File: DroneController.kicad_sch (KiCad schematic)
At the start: 50 parts, among them J1 Connector, J2 Connector, J3 Connector, P1 USB_C_Plug, Q2 AO3400A, SW1 SW_SPDT, U2 W25Q16JVSS, U3 BMP280, U4 MPU-6500, U6 L86-M33, U7 915MHz, U9 AP7361C-33E, X1 X322512MSB4SI

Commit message: Fixed GPS wiring
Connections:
- net 3.3V is gone; now on net +3.3V: U6.4 (VCC)
- net USART1_RX renamed MCU_RX1
- net MCU_RX1: now also U6.2 (TXD1); no longer U6.1 (RXD1)
- net USART1_TX renamed MCU_TX1
- net MCU_TX1: now also U6.1 (RXD1); no longer U6.2 (TXD1)
- net USART2_RX renamed MCU_RX2
- net MCU_RX2: now also J1.2 (Pin_2); no longer J1.1 (Pin_1)
- net USART2_TX renamed MCU_TX2
- net MCU_TX2: now also J1.1 (Pin_1); no longer J1.2 (Pin_2)
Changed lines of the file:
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@@
 	)
 	(junction
-		(at 60.96 25.4)
-		(diameter 0)
-		(color 0 0 0 0)
-	)
-	(junction
 		(at 157.48 40.64)
 		(diameter 0)
@@
 	)
 	(junction
+		(at 62.23 25.4)
+		(diameter 0)
+		(color 0 0 0 0)
+	)
+	(junction
 		(at 161.29 123.19)
 		(diameter 0)
@@
 	(wire
 		(pts
-			(xy 60.96 22.86) (xy 60.96 25.4)
+			(xy 62.23 22.86) (xy 62.23 25.4)
 		)
 		(stroke
@@
 	(wire
 		(pts
+			(xy 62.23 22.86) (xy 60.96 22.86)
+		)
+		(stroke
+			(width 0)
+			(type default)
+		)
+	)
+	(wire
+		(pts
 			(xy 217.17 104.14) (xy 220.98 104.14)
 		)
@@
 	(wire
 		(pts
+			(xy 147.32 72.39) (xy 137.16 72.39)
+		)
+		(stroke
+			(width 0)
+			(type default)
+		)
+	)
+	(wire
+		(pts
 			(xy 53.34 93.98) (xy 53.34 91.44)
 		)
@@
 		)
 	)
+	(wire
+		(pts
+			(xy 62.23 25.4) (xy 60.96 25.4)
+		)
+		(stroke
+			(width 0)
+			(type default)
+		)
+	)
 	(polyline
 		(pts
@@
 		)
 	)
-	(wire
-		(pts
-			(xy 62.23 25.4) (xy 60.96 25.4)
-		)
-		(stroke
-			(width 0)
-			(type default)
-		)
-	)
 	(polyline
 		(pts
@@
 		)
 	)
-	(label "USART1_RX"
+	(label "MCU_TX1"
 		(at 50.8 83.82 0)
 		(effects
@@
 		)
 	)
+	(label "MCU_TX1"
+		(at 266.7 38.1 0)
+		(effects
+			(font
+				(size 1.27 1.27)
+			)
+			(justify left bottom)
+		)
+	)
 	(label "SPI5_NSS"
 		(at 266.7 50.8 0)
@@
 		)
 	)
+	(label "MCU_RX2"
+		(at 189.23 129.54 180)
+		(effects
+			(font
+				(size 1.27 1.27)
+			)
+			(justify right bottom)
+		)
+	)
 	(label "SPI2_SCK"
 		(at 266.7 22.86 0)
@@
 		)
 	)
-	(label "USART2_RX"
+	(label "MCU_RX1"
+		(at 50.8 86.36 0)
+		(effects
+			(font
+				(size 1.27 1.27)
+			)
+			(justify left bottom)
+		)
+	)
+	(label "MCU_RX2"
 		(at 266.7 88.9 0)
 		(effects
@@
 		)
 	)
-	(label "USART1_TX"
-		(at 266.7 38.1 0)
-		(effects
-			(font
-				(size 1.27 1.27)
-			)
-			(justify left bottom)
-		)
-	)
 	(label "SPI1_NSS"
 		(at 104.14 125.73 180)
@@
 		)
 	)
-	(label "USART1_RX"
-		(at 266.7 35.56 0)
-		(effects
-			(font
-				(size 1.27 1.27)
-			)
-			(justify left bottom)
-		)
-	)
 	(label "SPI1_NSS"
 		(at 266.7 86.36 0)
@@
 		)
 	)
-	(label "USART2_TX"
+	(label "MCU_TX2"
 		(at 266.7 91.44 0)
 		(effects
@@
 		)
 	)
-	(label "USART2_RX"
+	(label "MCU_TX2"
 		(at 189.23 127 180)
 		(effects
@@
 		)
 	)
-	(label "USART2_TX"
-		(at 189.23 129.54 180)
+	(label "MCU_RX1"
+		(at 266.7 35.56 0)
 		(effects
 			(font
 				(size 1.27 1.27)
 			)
-			(justify right bottom)
+			(justify left bottom)
 		)
 	)
@@
 		)
 	)
-	(label "USART1_TX"
-		(at 50.8 86.36 0)
-		(effects
-			(font
-				(size 1.27 1.27)
-			)
-			(justify left bottom)
-		)
-	)
 	(label "SPI1_MISO"
 		(at 248.92 135.89 180)
@@
 	)
 	(symbol
+		(lib_id "power:+3.3V")
+		(at 50.8 66.04 0)
+		(unit 1)
+		(exclude_from_sim no)
+		(in_bom yes)
+		(on_board yes)
+		(dnp no)
+		(fields_autoplaced yes)
+		(property "Reference" "#PWR035"
+			(at 50.8 69.85 0)
+			(effects
+				(font
+					(size 1.27 1.27)
+				)
+				(hide yes)
+			)
+		)
+		(property "Value" "+3.3V"
+			(at 50.8 60.96 0)
+			(effects
+				(font
+					(size 1.27 1.27)
+				)
+			)
+		)
+		(property "Footprint" ""
+			(at 50.8 66.04 0)
+			(effects
+				(font
+					(size 1.27 1.27)
+				)
+				(hide yes)
+			)
+		)
+		(property "Datasheet" ""
+			(at 50.8 66.04 0)
+			(effects
+				(font
+					(size 1.27 1.27)
+				)
+				(hide yes)
+			)
+		)
+		(property "Description" "Power symbol creates a global label with name \"+3.3V\""
+			(at 50.8 66.04 0)
+			(effects
+				(font
+					(size 1.27 1.27)
+				)
+				(hide yes)
+			)
+		)
+		(pin "1"
+		)
+		(instances
+			(project "DroneController"
+				(path "/89a72cea-fd24-4c2f-bde8-6b43291d77f4"
+					(reference "#PWR035")
+					(unit 1)
+				)
+			)
+		)
+	)
+	(symbol
 		(lib_name "0402,100nF_1")
 		(lib_id "PCM_JLCPCB-Capacitors:0402,100nF")
@@
 	)
 	(symbol
-		(lib_id "power:+BATT")
-		(at 50.8 66.04 0)
-		(unit 1)
-		(exclude_from_sim no)
-		(in_bom yes)
-		(on_board yes)
-		(dnp no)
-		(property "Reference" "#PWR042"
-			(at 50.8 69.85 0)
-			(effects
-				(font
-					(size 1.27 1.27)
-				)
-				(hide yes)
-			)
-		)
-		(property "Value" "3.3V"
-			(at 50.8 60.96 0)
-			(effects
-				(font
-					(size 1.27 1.27)
-				)
-			)
-		)
-		(property "Footprint" ""
-			(at 50.8 66.04 0)
-			(effects
-				(font
-					(size 1.27 1.27)
-				)
-				(hide yes)
-			)
-		)
-		(property "Datasheet" ""
-			(at 50.8 66.04 0)
-			(effects
-				(font
-					(size 1.27 1.27)
-				)
-				(hide yes)
-			)
-		)
-		(property "Description" "Power symbol creates a global label with name \"+BATT\""
-			(at 50.8 66.04 0)
-			(effects
-				(font
-					(size 1.27 1.27)
-				)
-				(hide yes)
-			)
-		)
-		(pin "1"
-		)
-		(instances
-			(project "DroneController"
-				(path "/89a72cea-fd24-4c2f-bde8-6b43291d77f4"
-					(reference "#PWR042")
-					(unit 1)
-				)
-			)
-		)
-	)
-	(symbol
 		(lib_id "PCM_JLCPCB-Capacitors:0402,100nF")
 		(at 158.75 55.88 270)
@@
 	(symbol
 		(lib_id "power:+3.3V")
-		(at 137.16 72.39 0)
+		(at 147.32 72.39 0)
 		(unit 1)
 		(exclude_from_sim no)
@@
 		(dnp no)
 		(property "Reference" "#PWR044"
-			(at 137.16 76.2 0)
+			(at 147.32 76.2 0)
 			(effects
 				(font
@@
 		)
 		(property "Value" "+3.3V"
-			(at 137.16 68.072 0)
+			(at 147.32 68.072 0)
 			(effects
 				(font
@@
 		)
 		(property "Footprint" ""
-			(at 137.16 72.39 0)
+			(at 147.32 72.39 0)
 			(effects
 				(font
@@
 		)
 		(property "Datasheet" ""
-			(at 137.16 72.39 0)
+			(at 147.32 72.39 0)
 			(effects
 				(font
@@
 		)
 		(property "Description" "Power symbol creates a global label with name \"+3.3V\""
-			(at 137.16 72.39 0)
+			(at 147.32 72.39 0)
 			(effects
 				(font

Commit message: DroneController: Improved clarity of silkscreen and added manual reset test pad for the MCU.
ESC Board: Modified Buck Converter, added SWD debugging, added ICs for BLDC control
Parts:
- removed R6: 75Ω, PCM_JLCPCB:R_0603, symbol PCM_JLCPCB-Resistors:0603,75Ω
- added R11: 200Ω, PCM_JLCPCB:R_0402, symbol PCM_JLCPCB-Resistors:0402,200Ω
- added TP1, TP2: TestPoint, symbol Connector:TestPoint
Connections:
- net +5V: now also R11.1
- net GND: now also TP2.1
- net at C27.1, U5.7 (NRST): now also TP1.1
- net at D3.2: now also R11.2
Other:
- note added: "Drone Controller"
- note removed: "Flight Controller"

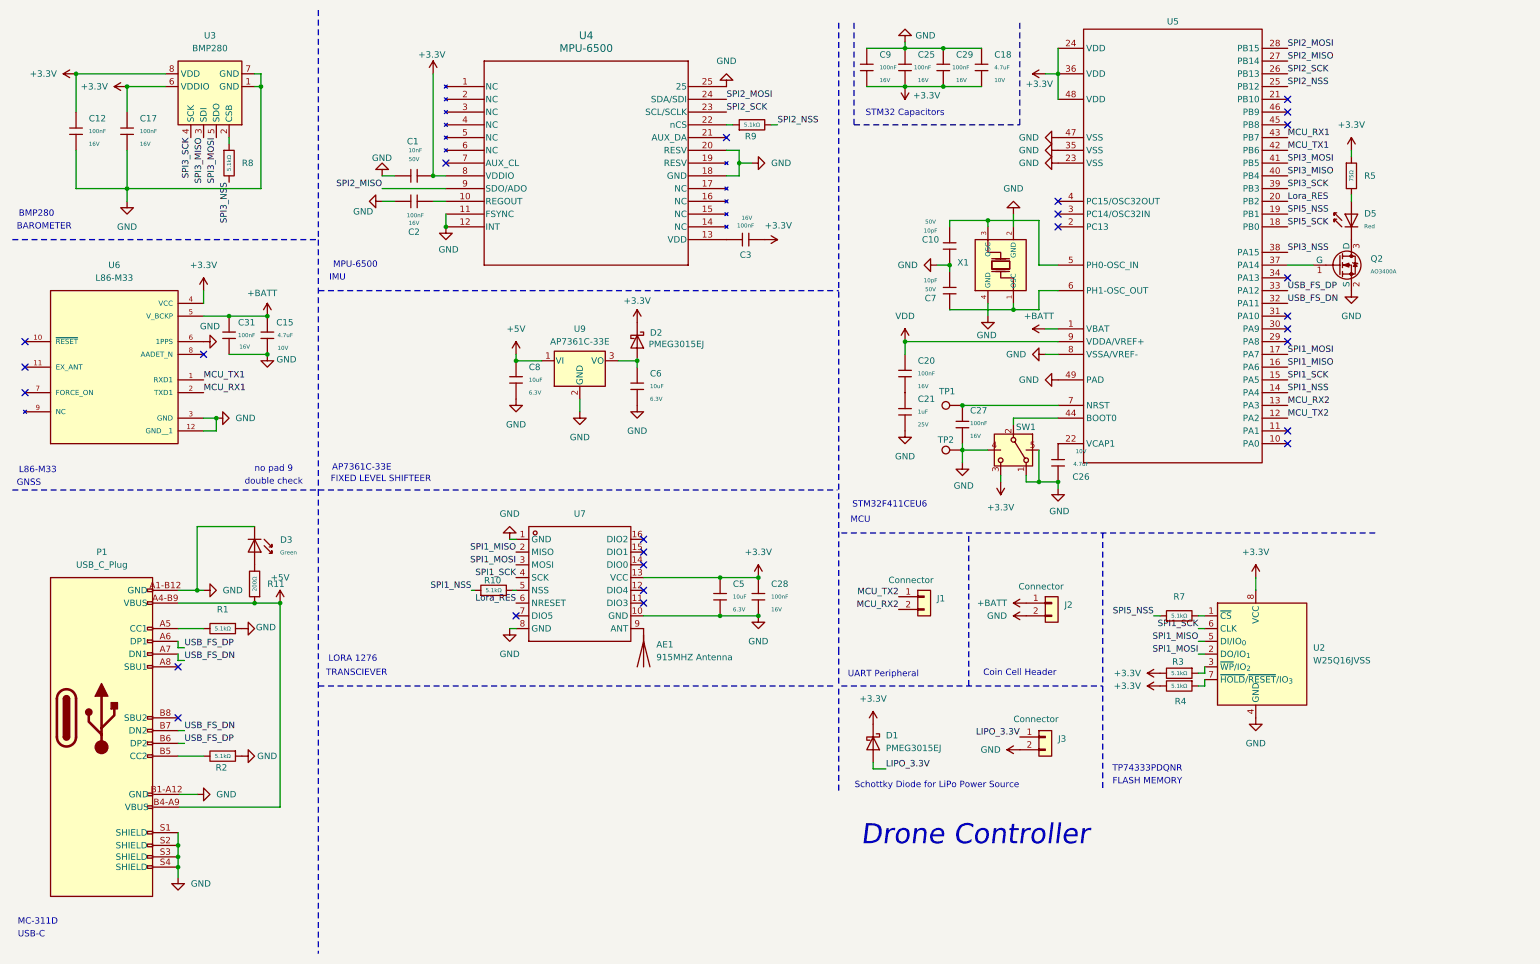
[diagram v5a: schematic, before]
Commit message: Added UART debugging for DroneController, repecced crystal oscillator.
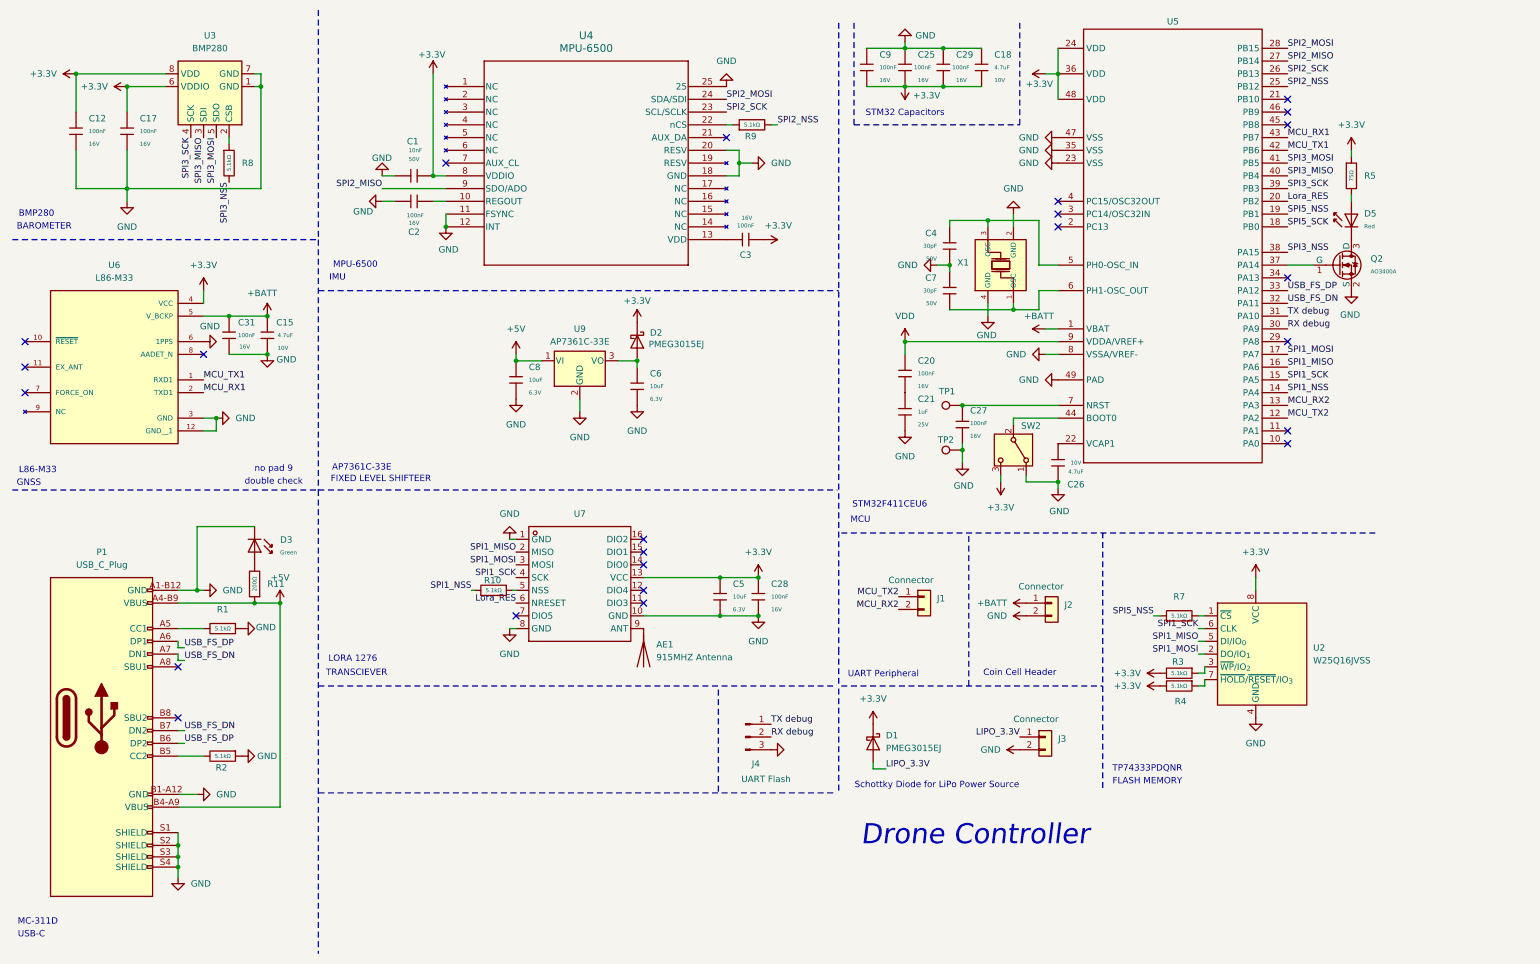
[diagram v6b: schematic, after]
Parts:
- removed C10, C7: 10pF, PCM_JLCPCB:C_0402, symbol PCM_JLCPCB-Capacitors:0402,10pF
- removed SW1: SW_SPDT, Switches:SW-SMD_MSK12CO2, symbol Switch:SW_SPDT
- added C4, C7: 30pF, PCM_JLCPCB:C_0402, symbol PCM_JLCPCB-Capacitors:0402,30pF
- added J4: UART Flash, Connector_PinHeader_1.00mm:PinHeader_1x03_P1.00mm_Vertical, symbol Connector:Conn_01x03_Pin
- added SW2: SW_SPDT, symbol Switch:SW_SPDT
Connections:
- net +3.3V: now also SW2.3 (C)
- net GND: now also C4.2, C7.1, J4.3 (Pin_3), SW2.1 (A)
- net at U5.6 (PH1-OSC_OUT), X1.1 (OSC): now also C7.2
- net at U5.5 (PH0-OSC_IN), X1.3 (OSC): now also C4.1
- net RX debug : now reaches U5.30 (PA9)
- net RX debug : now also J4.2 (Pin_2)
- net TX debug : now reaches U5.31 (PA10)
- net TX debug : now also J4.1 (Pin_1)
- net at U5.44 (BOOT0): now also SW2.2 (B)
- no-connect marks 26 -> 24

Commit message: DroneController: Adjusted crystal oscillator, added SWD debugging
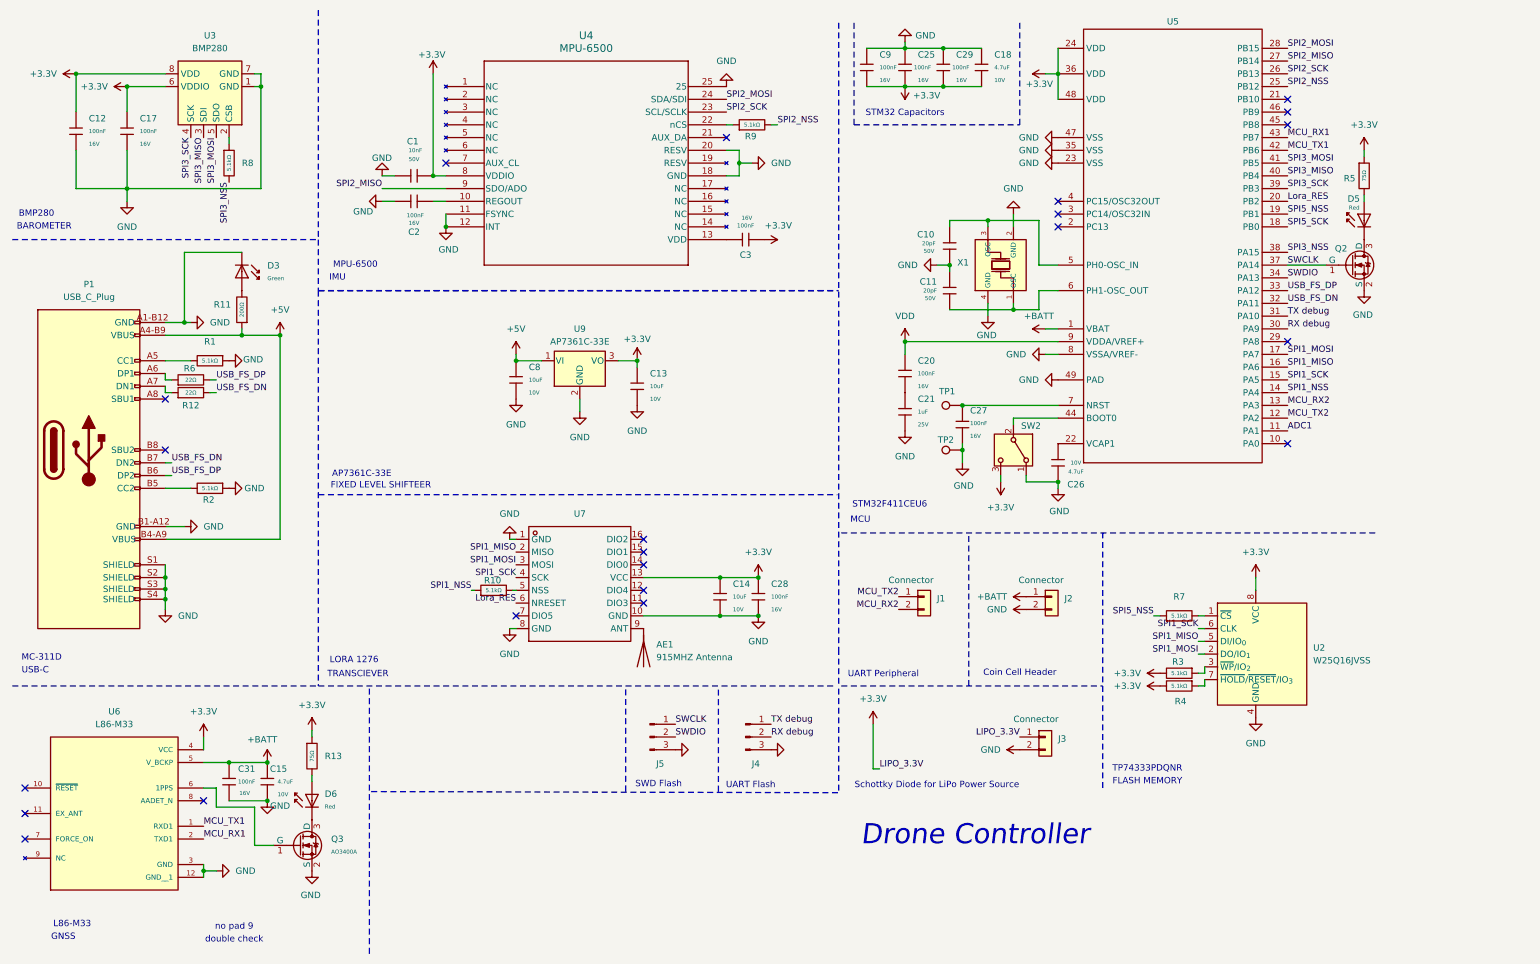
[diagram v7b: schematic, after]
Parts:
- removed C4, C7: 30pF, PCM_JLCPCB:C_0402, symbol PCM_JLCPCB-Capacitors:0402,30pF
- removed C5, C6: 10uF, PCM_JLCPCB:C_0402, symbol PCM_JLCPCB-Capacitors:0402,10uF
- removed D1, D2: PMEG3015EJ, Diode_SMD:D_SOD-323F, symbol Diode:PMEG3015EJ
- added C10, C11: 20pF, PCM_JLCPCB:C_0402, symbol PCM_JLCPCB-Capacitors:0402,20pF
- added C13, C14: 10uF, PCM_JLCPCB:C_0402, symbol PCM_JLCPCB-Capacitors:0402,10uF
- added D6: Red, PCM_JLCPCB:D_0805, symbol PCM_JLCPCB-Diodes:LED,0805,Red
- added J5: UART Flash, Connector_PinHeader_1.00mm:PinHeader_1x03_P1.00mm_Vertical, symbol Connector:Conn_01x03_Pin
- added Q3: AO3400A, PCM_JLCPCB:Q_SOT-23, symbol PCM_JLCPCB-Transistors:NMOS,AO3400A
- added R12, R6: 22Ω, PCM_JLCPCB:R_0402, symbol PCM_JLCPCB-Resistors:0402,22Ω
- added R13: 75Ω, PCM_JLCPCB:R_0603, symbol PCM_JLCPCB-Resistors:0603,75Ω
- C8: Attrition Qty 10 -> (none); Class Basic Component -> (none); LCSC C15525 -> C19702; Minimum Qty 20 -> (none); Part CL05A106MQ5NUNC -> (none); Price 0.007USD -> (none); Process SMT -> (none); Stock 3423130 -> (none); Tolerance ±20% -> (none); Voltage Rated 6.3V -> 10V
- X1: value X322512MSB4SI -> Shenzhen SCTF Elec SX2B12.000F1010F30; Attrition Qty 4 -> (none); Category Crystals/Oscillators/Resonators,Crystals -> (none); Class Basic Component -> (none); LCSC C9002 -> C7301971; Load Capacitance 20pF -> 10pf; Manufacturer Yangxing Tech -> (none); Minimum Qty 5 -> (none); Price 0.069USD -> (none); Process SMT -> (none); Stock 88445 -> (none)
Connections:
- net LIPO_3.3V is gone; now on net +3.3V: J3.1 (Pin_1)
- net +3.3V: now also U9.3 (VO), C13.1, C14.1, R13.1
- net GND: now also C10.2, C11.1, C13.2, C14.2, J5.3 (Pin_3), Q3.2 (S); no longer U6.6 (1PPS)
- net USB_FS_DN: now also R12.2; no longer P1.A7 (DN1)
- net USB_FS_DP: now also R6.2; no longer P1.A6 (DP1)
- net at U5.6 (PH1-OSC_OUT), X1.1 (OSC): now also C11.2
- net at U5.5 (PH0-OSC_IN), X1.3 (OSC): now also C10.1
- net ADC1: now reaches U5.11 (PA1)
- net SWDIO: now reaches U5.34 (PA13)
- net SWDIO: now also J5.2 (Pin_2)
- net SWCLK: now reaches Q2.1 (G), U5.37 (PA14)
- net SWCLK: now also J5.1 (Pin_1)
- new net: P1.A6 (DP1), R6.1
- new net: P1.A7 (DN1), R12.1
- new net: Q3.1 (G), U6.6 (1PPS)
- new net: D6.1, Q3.3 (D)
- new net: D6.2, R13.2
- no-connect marks 24 -> 22
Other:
- note added: "SWD Flash"
- note added: "UART Flash"
- moved on the sheet: C15, C31, D3, D5, J2, P1, Q2, R1, R11, R2, R5, U6
